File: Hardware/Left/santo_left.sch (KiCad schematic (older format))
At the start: 14 parts, among them J1 USB_C_Receptacle, J2 USB_C_Receptacle, SW1 SW_Push, U1 ATMEGA32U4-MU

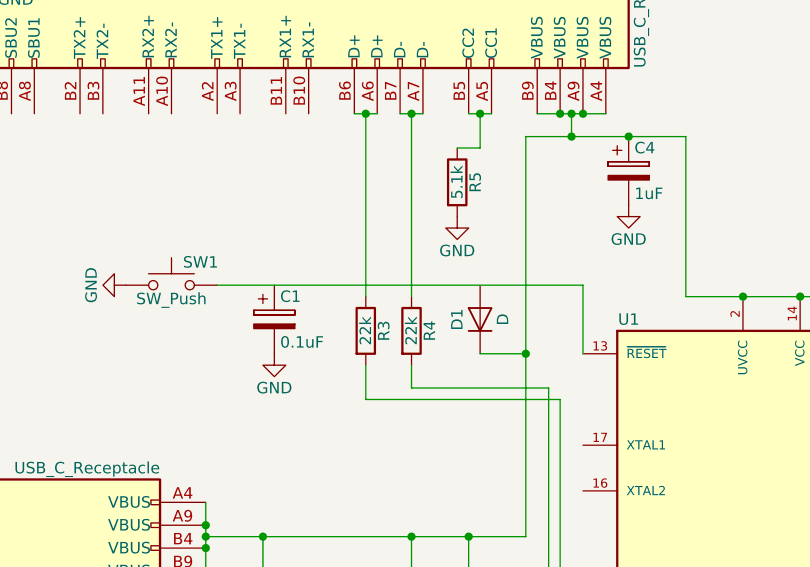
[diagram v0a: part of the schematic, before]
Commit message: Fixup reset circuit
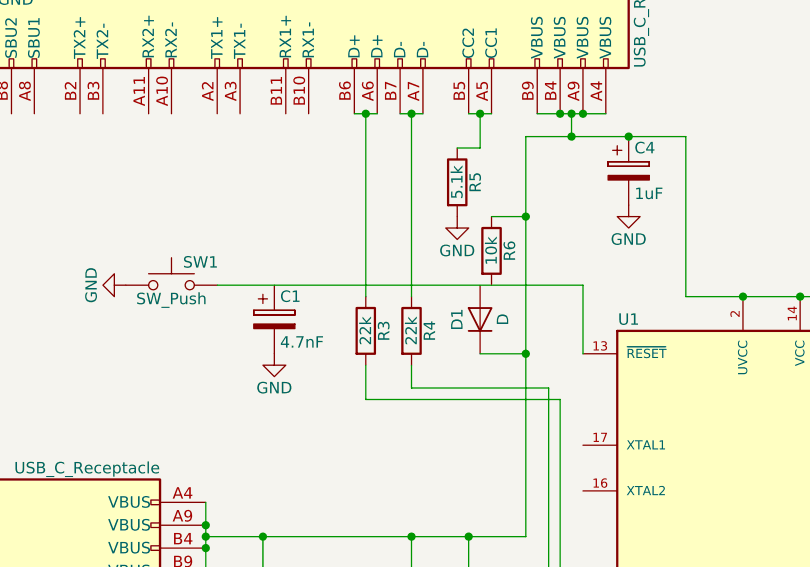
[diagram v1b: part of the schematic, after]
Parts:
- added R6: 10k, symbol R
- C1: value 0.1uF -> 4.7nF
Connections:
- net at C2.1, C4.1, D1.1 (K)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: now also R6.1
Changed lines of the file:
@@
 P 2200 2600
 F 0 "C1" H 2225 2700 50  0000 L CNN
-F 1 "0.1uF" H 2225 2500 50  0000 L CNN
+F 1 "4.7nF" H 2225 2500 50  0000 L CNN
 F 2 "" H 2238 2450 50  0001 C CNN
 F 3 "" H 2200 2600 50  0001 C CNN
@@
 	3100 2750 3300 2750
 Connection ~ 3300 2750
+$Comp
+L R R6
+U 1 1 5A09E449
+P 3150 2300
+F 0 "R6" V 3230 2300 50  0000 C CNN
+F 1 "10k" V 3150 2300 50  0000 C CNN
+F 2 "" V 3080 2300 50  0001 C CNN
+F 3 "" H 3150 2300 50  0001 C CNN
+	1    3150 2300
+	1    0    0    -1
+$EndComp
+Wire Wire Line
+	3150 2150 3300 2150
+Connection ~ 3300 2150
 $EndSCHEMATC

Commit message: fixup schematic; wip
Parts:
- removed C1: 4.7nF, symbol CP
- removed C2: 10uF, symbol CP
- removed C3, C4: 1uF, symbol CP
- removed D1: D, symbol D
- removed J1, J2: USB_C_Receptacle, symbol USB_C_Receptacle
- removed R1, R2: 4.7k, symbol R
- removed R3, R4: 22k, symbol R
- removed R5: 5.1k, symbol R
- removed R6: 10k, symbol R
- removed SW1: SW_Push, symbol SW_Push
- removed U1: ATMEGA32U4-MU, QFN44, symbol ATMEGA32U4-MU
- added C? (x2): 22pF, symbol C
- added C?: 10uF, symbol CP_Small
- added C? (x4): 0.1uF, symbol C_Small
- added C?: 1uF, symbol C_Small
- added J? (x2): USB_C_Receptacle, symbol USB_C_Receptacle
- added R? (x2): 10k, symbol R_Small
- added R? (x2): 5.1k, symbol R_Small
- added R? (x2): 22, symbol R_Small
- added R? (x2): 4.7k, symbol R_Small
- added SW?: SW_Push, symbol SW_Push
- added U?: ATMEGA32U4RC-MU, QFN44, symbol ATMEGA32U4RC-MU
- added Y?: 16MHz, symbol Crystal
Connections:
- net GND: now also C?.2, C?.2, C?.2, C?.2, C?.2, C?.2, C?.2, C?.2, J?.A1 (GND), J?.A1 (GND), J?.A12 (GND), J?.A12 (GND), J?.B1 (GND), J?.B1 (GND), J?.B12 (GND), J?.B12 (GND), J?.S1 (SHIELD), J?.S1 (SHIELD), R?.2, R?.2, R?.2, SW?.1, U?.15 (GND), U?.23 (GND), U?.35 (GND), U?.43 (GND), U?.5 (UGND)
- net SCL: now also J?.A7 (D-), J?.B7 (D-), R?.2, U?.18 ((OC0B/SCL/INT0)PD0)
- net SDA: now also J?.A6 (D+), J?.B6 (D+), R?.1, U?.19 ((SDA/INT1)PD1)
- new net: J?.A5 (CC1), R?.1
- new net: J?.A6 (D+), J?.B6 (D+), R?.1
- new net: J?.A7 (D-), J?.B7 (D-), R?.1
- new net: J?.B5 (CC2), R?.1
- new net D+: R?.2, U?.4 (D+)
- new net D-: R?.2, U?.3 (D-)
- new net HWB_PE2: R?.1, U?.33 ((~HWB~)PE2)
- new net RESET: R?.2, SW?.2, U?.13 (~RESET~)
- new net UCAP: C?.1, U?.6 (UCAP)
- new net VCC: C?.1, C?.1, C?.1, C?.1, C?.1, J?.A4 (VBUS), J?.A4 (VBUS), J?.A9 (VBUS), J?.A9 (VBUS), J?.B4 (VBUS), J?.B4 (VBUS), J?.B9 (VBUS), J?.B9 (VBUS), R?.1, R?.1, R?.2, U?.14 (VCC), U?.2 (UVCC), U?.24 (AVCC), U?.34 (VCC), U?.44 (AVCC), U?.7 (VBUS)
- new net XTAL1: C?.1, U?.17 (XTAL1), Y?.1
- new net XTAL2: C?.1, U?.16 (XTAL2), Y?.2
- no-connect marks 0 -> 23
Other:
- note added: "Board to Board"
- note added: "Computer to Board"
- note removed: "Board <-> Board COM"
- note removed: "Computer <-> Microcontroller COM"

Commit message: finish schematic
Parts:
- added D1, D10, D11, D12, D13, D14, D15, D16, D17, D18, D19, D2, D20, D3, D4, D5, D6, D7, D8, D9: D_Small, symbol D_Small
- added SW1, SW10, SW11, SW12, SW13, SW14, SW15, SW16, SW18, SW19, SW2, SW20, SW21, SW3, SW4, SW5, SW6, SW7, SW8, SW9: SW_Push, symbol SW_Push
- gave numbers to parts that had none: 21
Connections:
- net ROW_2: now reaches U1.10 ((PDI/MOSI/PCINT2)PB2)
- net ROW_2: now also D11.1 (K), D15.1 (K), D19.1 (K), D3.1 (K), D7.1 (K)
- net ROW_3: now reaches U1.11 ((PDO/MISO/PCINT3)PB3)
- net ROW_3: now also D12.1 (K), D16.1 (K), D20.1 (K), D4.1 (K), D8.1 (K)
- net COL_3: now reaches U1.12 ((OC0A/OC1C/~RTS~/PCINT7)PB7)
- net COL_3: now also SW13.2, SW14.2, SW15.2, SW16.2
- net COL_0: now reaches U1.28 ((ADC11/PCINT4)PB4)
- net COL_0: now also SW1.2, SW2.2, SW3.2, SW4.2
- net COL_1: now reaches U1.29 ((ADC12/OC1A/~OC4B~/PCINT12)PB5)
- net COL_1: now also SW5.2, SW6.2, SW7.2, SW8.2
- net COL_2: now reaches U1.30 ((ADC13/OC1B/OC4B/PCINT13)PB6)
- net COL_2: now also SW10.2, SW11.2, SW12.2, SW9.2
- net ROW_0: now reaches U1.8 ((SS/PCINT0)PB0)
- net ROW_0: now also D1.1 (K), D13.1 (K), D17.1 (K), D5.1 (K), D9.1 (K)
- net ROW_1: now reaches U1.9 ((SCLK/PCINT1)PB1)
- net ROW_1: now also D10.1 (K), D14.1 (K), D18.1 (K), D2.1 (K), D6.1 (K)
- new net: D1.2 (A), SW1.1
- new net: D5.2 (A), SW5.1
- new net: D9.2 (A), SW9.1
- new net: D13.2 (A), SW13.1
- new net: D17.2 (A), SW18.1
- new net: D2.2 (A), SW2.1
- new net: D6.2 (A), SW6.1
- new net: D10.2 (A), SW10.1
- new net: D14.2 (A), SW14.1
- new net: D18.2 (A), SW19.1
- new net: D3.2 (A), SW3.1
- new net: D7.2 (A), SW7.1
- new net: D11.2 (A), SW11.1
- new net: D19.2 (A), SW20.1
- new net: D4.2 (A), SW4.1
- new net: D8.2 (A), SW8.1
- new net: D12.2 (A), SW12.1
- new net: D16.2 (A), SW16.1
- new net: D20.2 (A), SW21.1
- new net COL_4: SW18.2, SW19.2, SW20.2, SW21.2
- no-connect marks 23 -> 38

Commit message: fix some bugs
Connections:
- net COL_4: now also U1.31 ((OC3A/~OC4A~)PC6)
- net at SW15.1: now also D15.2 (A)
- no-connect marks 38 -> 37

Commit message: Add new schematic for crystal
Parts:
- removed C1, C2: 22pF, symbol C
- removed Y1: 16MHz, symbol Crystal
- added C1, C2: 6pF, symbol C_Small
- added Y1: 16MHz, symbol CX3225SB16000D0GZJC1
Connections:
- wire segments 204 -> 205
